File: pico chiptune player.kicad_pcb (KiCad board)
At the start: 4 copper layers, 80 x 70.8 mm, 32 parts, among them J1 MicroSD, J2 Spk Out, SW1 Play / Pause, SW2 Next, SW3 Previous, U1 AY-3-8910, U2 PAM8302AAS, U3 0.96"OLED_I2C

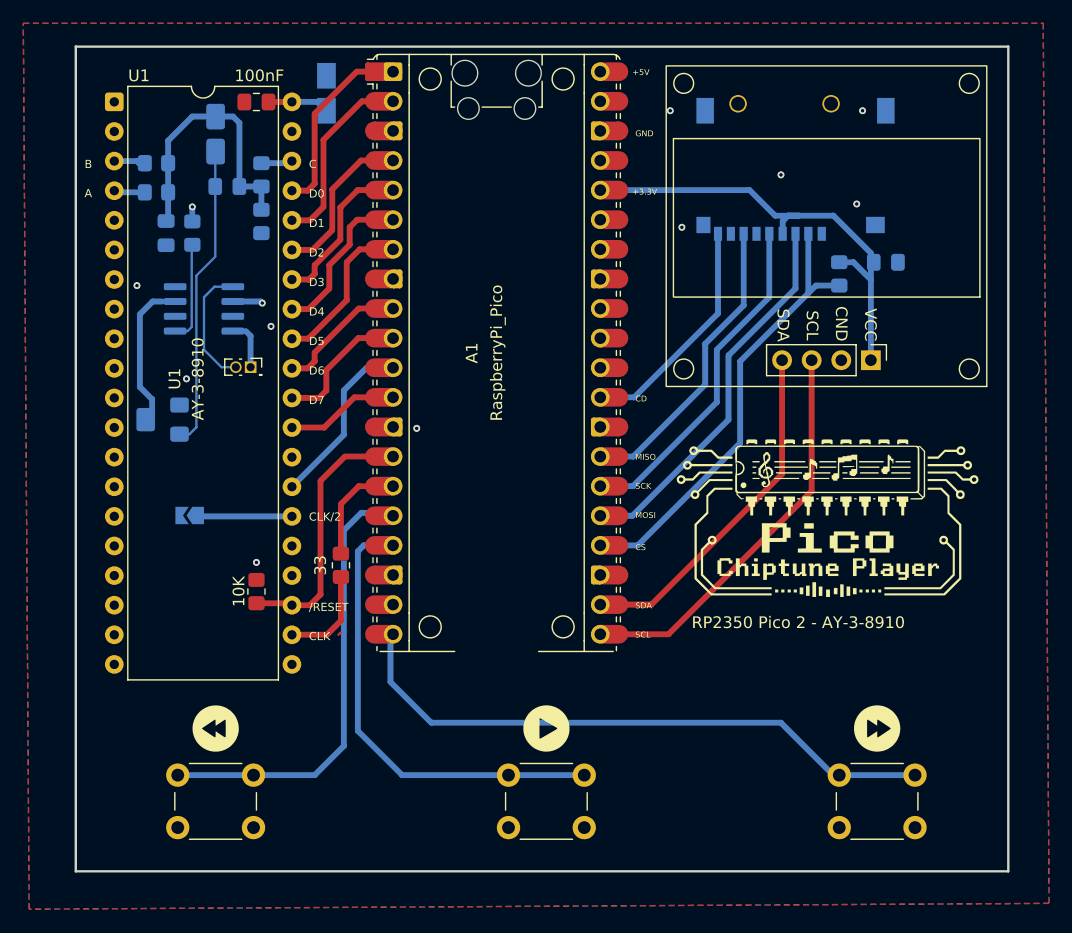
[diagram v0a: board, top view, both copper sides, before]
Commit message: pcb, dru: update silk text sizes to >=0.8mm for DRC compliance and add JLCPCB design rules
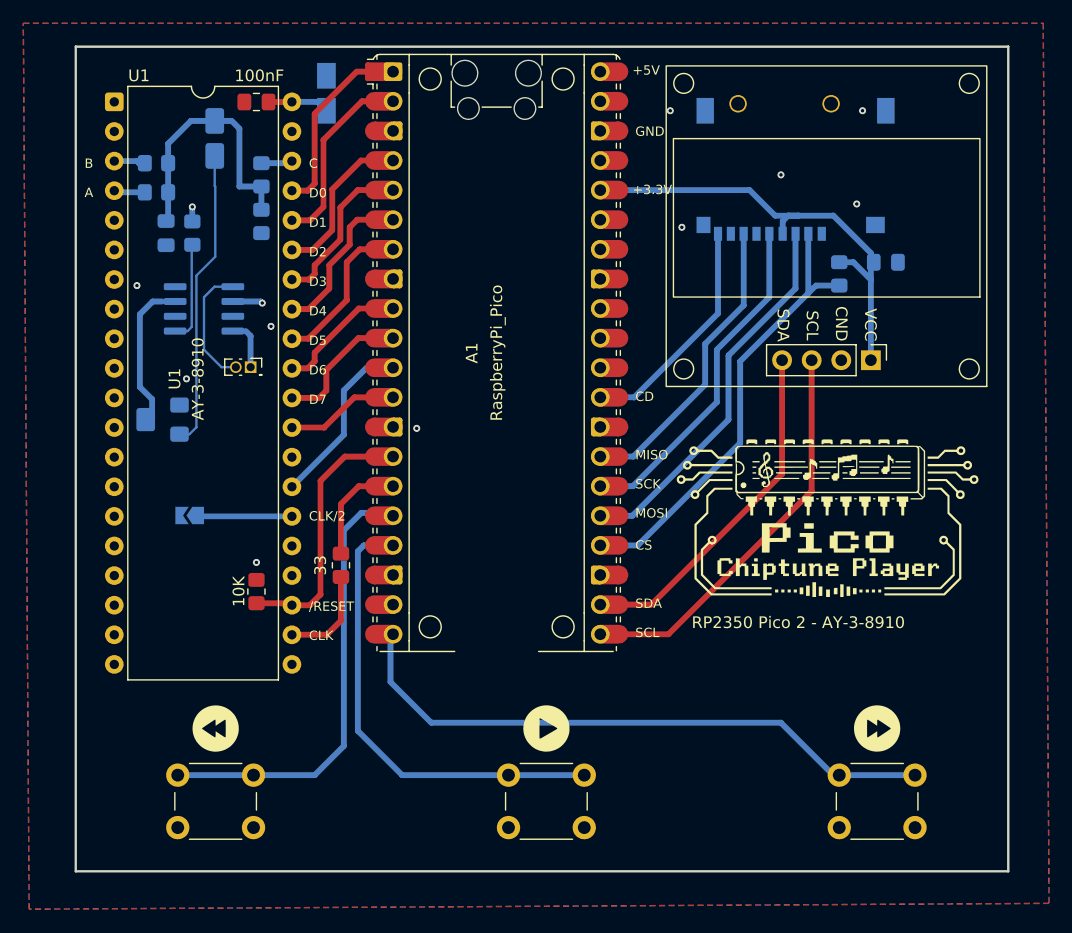
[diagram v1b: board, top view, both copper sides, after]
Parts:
- removed the C3 at (120.5, 80.0)
- removed the C3 at (121.5, 84.5)
- added C3: 1uF, Capacitor_SMD:CP_Elec_3x5.4, B.Cu at (120.4, 80.4)
- J1: renamed from J2; value Spk Out -> Speaker Out
- JP1: value CLLK DIV -> Clk Div
- renumbered C4 to C1, C5 to C2, C2 to C4, C1 to C5, J1 to J2, R3 to R1, R1 to R3, R8 to R6, R6 to R7, R7 to R8, U3 to U2, U2 to U3
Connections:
- U1 pad 24: +5V -> GND
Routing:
- net Net-(C3-Pad1): track 23.6 -> 22.8 mm
- net +5V: track 9.74 -> 9.11 mm
- net GND: track 0.00 -> 0.63 mm

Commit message: fix(dru): update JLCPCB custom design rules syntax for KiCad 10 compliance
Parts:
- A1: value RaspberryPi_Pico -> RaspberryPi_Pico 2
